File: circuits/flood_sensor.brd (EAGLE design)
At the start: 74 x 74 mm, 51 parts, among them T1 BC847, U1 MMA8452Q, U2 LM1117, U3 DS18B20, U5 LMV358

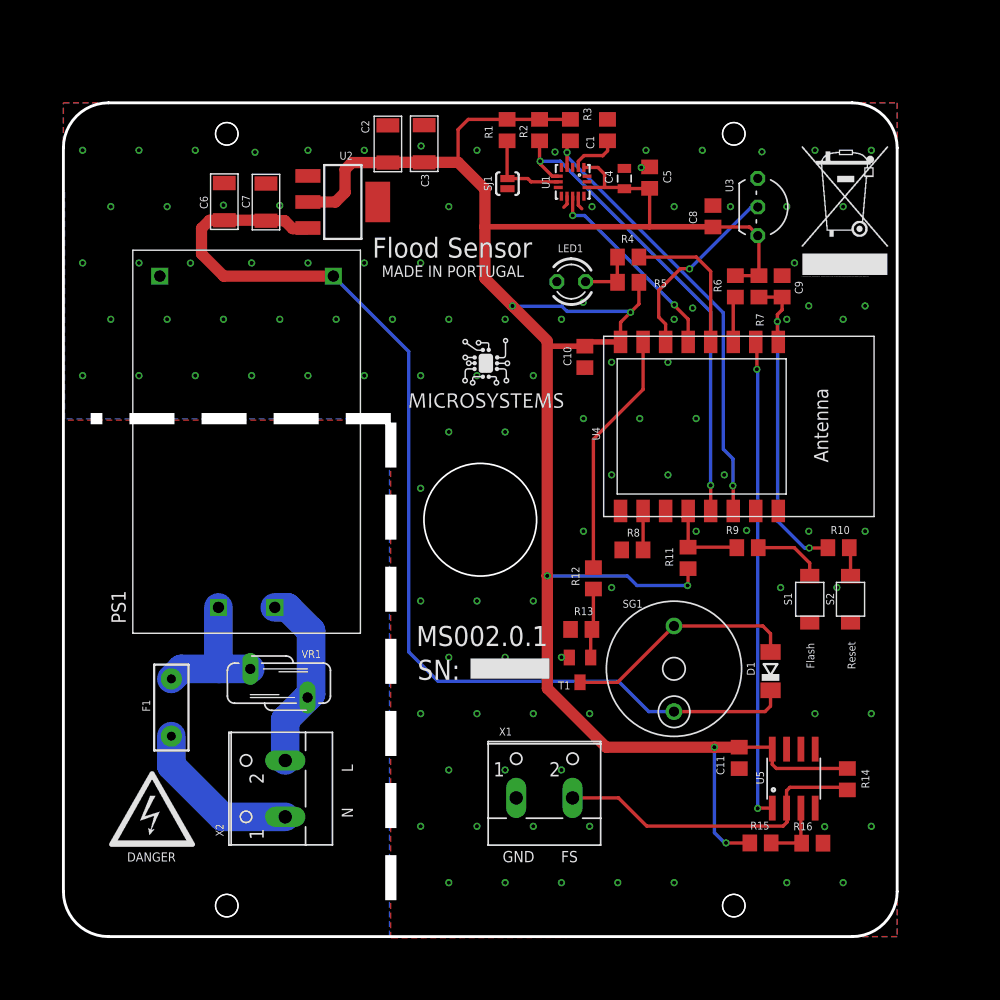
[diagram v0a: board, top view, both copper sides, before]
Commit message: remove copper close to outline
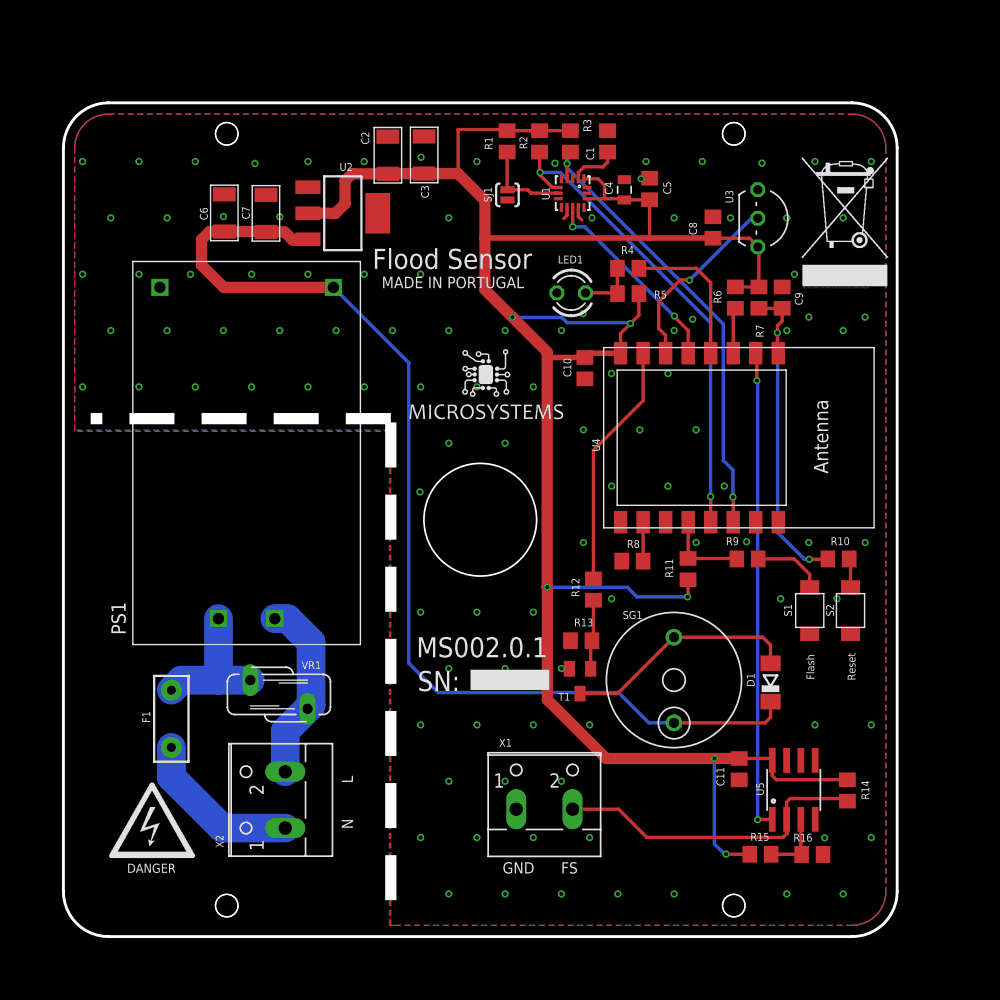
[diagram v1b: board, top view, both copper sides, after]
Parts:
- moved R15 1.00 mm to (61.9, 7.31)
- moved C1 1.00 mm to (48.3, 70.6)
- moved C10 1.00 mm to (46.3, 50.5)
- moved C11 1.00 mm to (60.0, 14.9)
- moved C2 1.00 mm to (28.8, 69.3)
- moved C3 1.00 mm to (32.0, 69.4)
- moved C4 1.00 mm to (49.8, 66.3)
- moved C5 1.00 mm to (52.0, 66.4)
- moved C6 1.00 mm to (14.3, 64.2)
- moved C7 1.00 mm to (18.0, 64.2)
- moved C8 1.00 mm to (57.6, 62.9)
- moved C9 1.00 mm to (63.8, 56.7)
- moved D1 1.00 mm to (62.8, 22.6)
- moved F1 1.00 mm to (9.58, 19.3)
- moved LED1 1.00 mm to (45.1, 57.1)
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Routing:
- net +3V3: track 201.2 -> 201.8 mm

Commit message: updated flood_sensor
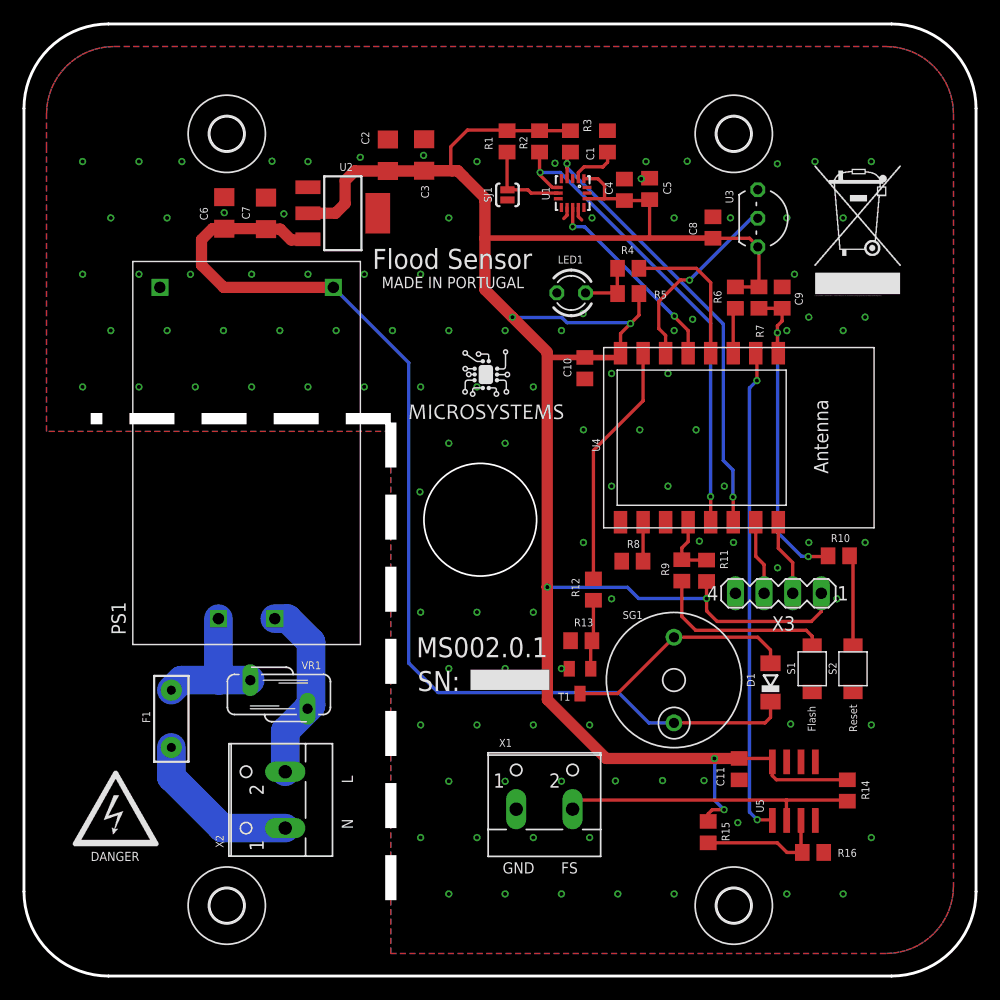
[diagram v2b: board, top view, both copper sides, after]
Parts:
- added X3: (no value), con-lstb:MA04-1
- C2, C3, C6, C7: device Seeed-Capacitor:C1206 -> rcl:C1206
- C4: device SparkFun:0805 -> rcl:C0805
- H1, H2, H3, H4: value MOUNT-HOLE -> MOUNT-HOLE3.0; device holes:2,0 -> holes:3,0
- SG1: value (none) -> BMT1205XH7.5
- U1: device SparkFun:QFN-16_0.5MM -> ruben:QFN-16_0.5MM
- U5: value LMV358 -> LMV358M; device SparkFun:SO08 -> linear:SO08
- moved R9 5.92 mm to (54.9, 32.5), turned to 270 degrees
- moved S1 5.17 mm to (66.5, 23.8)
- moved S2 5.17 mm to (70.1, 23.8)
- moved R15 5.04 mm to (57.2, 9.27), turned to 270 degrees
- moved U$3 3.40 mm to (0.85, 7.58)
- moved R11 1.65 mm to (57.1, 32.5)
- moved U$1 1.33 mm to (66.7, 57.0)
- moved R10 0.28 mm to (68.8, 33.8)
- moved R16 0.19 mm to (66.5, 7.47)
- moved U5 0.11 mm to (64.8, 12.9)
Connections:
- net +3V3: now also X3.1
- net ESP_RX: now also X3.3
- net ESP_TX: now also X3.2
- net GND: now also X3.4
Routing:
- net +3V3: track 201.8 -> 213.7 mm
- net N$6: track 6.29 -> 16.3 mm
- net ESP_TX: track 0.00 -> 6.84 mm
- net ESP_RX: track 0.00 -> 6.62 mm
- net N$2: track 5.85 -> 11.6 mm
- net N$9: track 2.57 -> 8.10 mm
- net N$8: track 28.6 -> 26.6 mm
- net GPIO0: track 7.57 -> 5.79 mm
- net FLOOD_ADC: track 42.8 -> 43.4 mm
- net GND: vias 105 -> 108
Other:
- board size 74 x 74 mm -> 84.5 x 84.5 mm

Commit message: corrected pcb dimensions
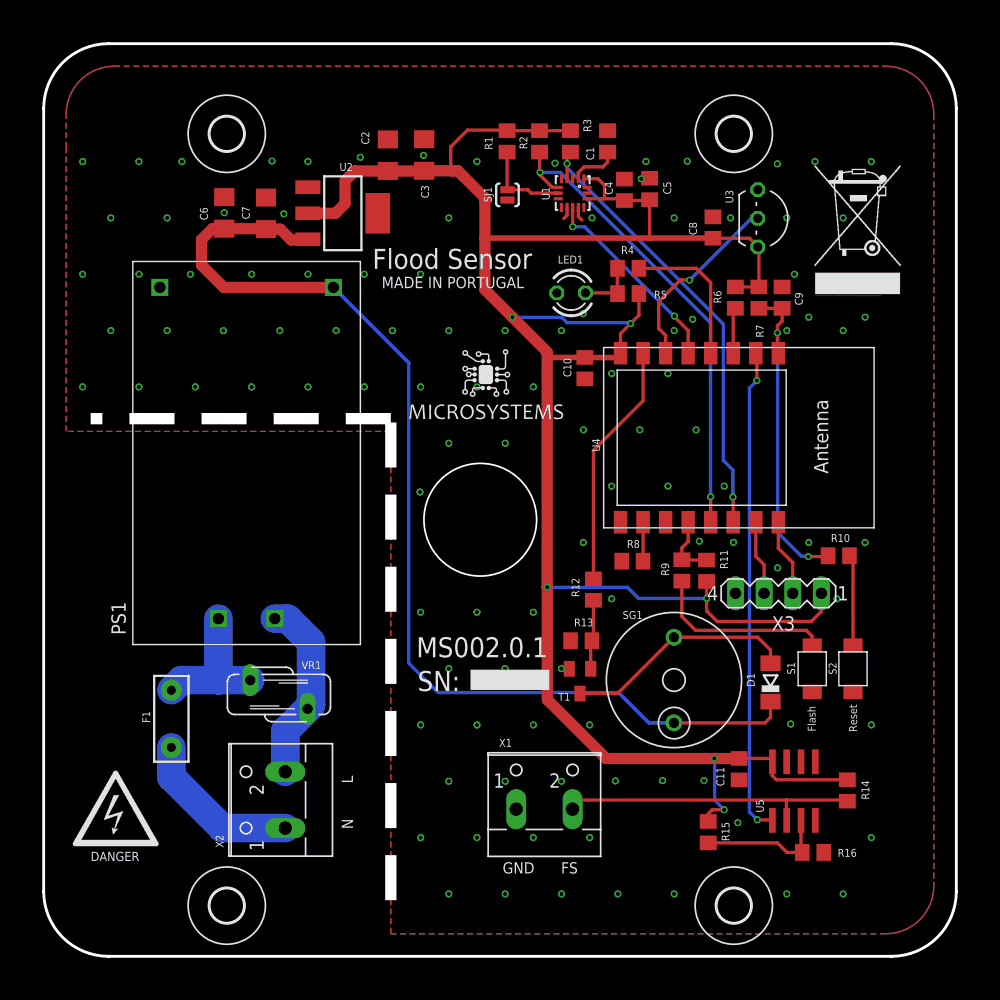
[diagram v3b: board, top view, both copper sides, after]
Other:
- board size 84.5 x 84.5 mm -> 81 x 81 mm

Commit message: finished first revision
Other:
- outline, holes or cut-outs redrawn
